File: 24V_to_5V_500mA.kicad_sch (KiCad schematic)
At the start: 6 parts, among them U4 R-78E5.0-0.5

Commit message: 24V updates
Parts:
- renumbered C30 to C10, C27 to C7, C28 to C8, C29 to C9, U4 to U2
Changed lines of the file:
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@@
   (symbol (lib_id "Device:C") (at 133.35 96.52 0) (unit 1)
     (in_bom yes) (on_board yes)
-    (property "Reference" "C28" (id 0) (at 136.271 95.3516 0)
+    (property "Reference" "C8" (id 0) (at 136.271 95.3516 0)
       (effects (font (size 1.27 1.27)) (justify left))
     )
@@
   (symbol (lib_id "Device:C") (at 123.19 96.52 0) (unit 1)
     (in_bom yes) (on_board yes)
-    (property "Reference" "C27" (id 0) (at 126.111 95.3516 0)
+    (property "Reference" "C7" (id 0) (at 126.111 95.3516 0)
       (effects (font (size 1.27 1.27)) (justify left))
     )
@@
   (symbol (lib_id "Device:C") (at 162.56 96.52 0) (unit 1)
     (in_bom yes) (on_board yes)
-    (property "Reference" "C29" (id 0) (at 165.481 95.3516 0)
+    (property "Reference" "C9" (id 0) (at 165.481 95.3516 0)
       (effects (font (size 1.27 1.27)) (justify left))
     )
@@
   (symbol (lib_id "Device:C") (at 175.26 96.52 0) (unit 1)
     (in_bom yes) (on_board yes)
-    (property "Reference" "C30" (id 0) (at 178.181 95.3516 0)
+    (property "Reference" "C10" (id 0) (at 178.181 95.3516 0)
       (effects (font (size 1.27 1.27)) (justify left))
     )
@@
   (symbol (lib_id "Regulator_Switching:R-78E5.0-0.5") (at 148.59 92.71 0) (unit 1)
     (in_bom yes) (on_board yes)
-    (property "Reference" "U4" (id 0) (at 148.59 86.5632 0))
+    (property "Reference" "U2" (id 0) (at 148.59 86.5632 0))
     (property "Value" "R-78E5.0-0.5" (id 1) (at 148.59 88.8746 0))
     (property "Footprint" "Converter_DCDC:Converter_DCDC_RECOM_R-78E-0.5_THT" (id 2) (at 149.86 99.06 0)
@@
   (symbol (lib_id "power:PWR_FLAG") (at 135.89 92.71 0) (unit 1)
     (in_bom yes) (on_board yes)
-    (property "Reference" "#FLG06" (id 0) (at 135.89 90.805 0)
+    (property "Reference" "#FLG05" (id 0) (at 135.89 90.805 0)
       (effects (font (size 1.27 1.27)) hide)
     )

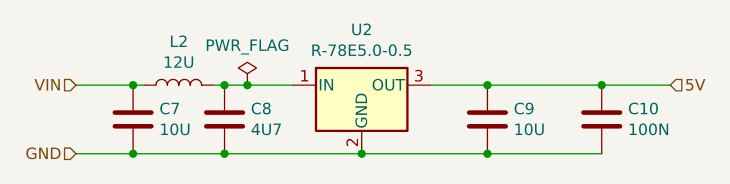
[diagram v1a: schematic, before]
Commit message: fix LT1161 symbol/sch
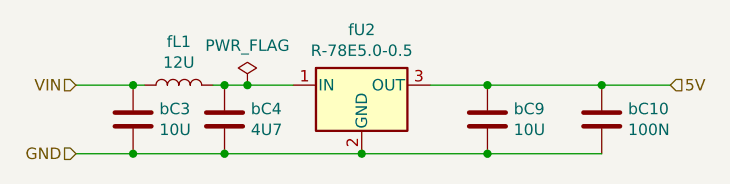
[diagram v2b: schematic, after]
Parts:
- renumbered C10 to bC10, C7 to bC3, C8 to bC4, C9 to bC9, L2 to fL1, U2 to fU2
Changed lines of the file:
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@@
   (symbol (lib_id "Device:L") (at 128.27 92.71 90) (unit 1)
     (in_bom yes) (on_board yes)
-    (property "Reference" "L2" (id 0) (at 128.27 87.884 90))
+    (property "Reference" "fL1" (id 0) (at 128.27 87.884 90))
     (property "Value" "12U" (id 1) (at 128.27 90.1954 90))
     (property "Footprint" "Inductor_THT:L_Radial_D8.7mm_P5.00mm_Fastron_07HCP" (id 2) (at 128.27 92.71 0)
@@
   (symbol (lib_id "Device:C") (at 133.35 96.52 0) (unit 1)
     (in_bom yes) (on_board yes)
-    (property "Reference" "C8" (id 0) (at 136.271 95.3516 0)
+    (property "Reference" "bC4" (id 0) (at 136.271 95.3516 0)
       (effects (font (size 1.27 1.27)) (justify left))
     )
@@
   (symbol (lib_id "Device:C") (at 123.19 96.52 0) (unit 1)
     (in_bom yes) (on_board yes)
-    (property "Reference" "C7" (id 0) (at 126.111 95.3516 0)
+    (property "Reference" "bC3" (id 0) (at 126.111 95.3516 0)
       (effects (font (size 1.27 1.27)) (justify left))
     )
@@
   (symbol (lib_id "Device:C") (at 162.56 96.52 0) (unit 1)
     (in_bom yes) (on_board yes)
-    (property "Reference" "C9" (id 0) (at 165.481 95.3516 0)
+    (property "Reference" "bC9" (id 0) (at 165.481 95.3516 0)
       (effects (font (size 1.27 1.27)) (justify left))
     )
@@
   (symbol (lib_id "Device:C") (at 175.26 96.52 0) (unit 1)
     (in_bom yes) (on_board yes)
-    (property "Reference" "C10" (id 0) (at 178.181 95.3516 0)
+    (property "Reference" "bC10" (id 0) (at 178.181 95.3516 0)
       (effects (font (size 1.27 1.27)) (justify left))
     )
@@
   (symbol (lib_id "Regulator_Switching:R-78E5.0-0.5") (at 148.59 92.71 0) (unit 1)
     (in_bom yes) (on_board yes)
-    (property "Reference" "U2" (id 0) (at 148.59 86.5632 0))
+    (property "Reference" "fU2" (id 0) (at 148.59 86.5632 0))
     (property "Value" "R-78E5.0-0.5" (id 1) (at 148.59 88.8746 0))
     (property "Footprint" "Converter_DCDC:Converter_DCDC_RECOM_R-78E-0.5_THT" (id 2) (at 149.86 99.06 0)
@@
   (symbol (lib_id "power:PWR_FLAG") (at 135.89 92.71 0) (unit 1)
     (in_bom yes) (on_board yes)
-    (property "Reference" "#FLG05" (id 0) (at 135.89 90.805 0)
+    (property "Reference" "#FLG04" (id 0) (at 135.89 90.805 0)
       (effects (font (size 1.27 1.27)) hide)
     )
